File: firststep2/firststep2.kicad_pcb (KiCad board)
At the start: 2 copper layers, 43.2 x 17.8 mm, 43 parts, among them J1 Analog, J10 Arduino_A7, J11 Arduino_D6, J12 RELAY_SW, J13 RELAY_PWR, J14 Arduino_D9, J15 Conn_FET, J2 Conn_01x03_Male, J2 Digital, J3 POWER12, J4 Conn_5V, J5 Conn_GND, J6 Arduino_A6, U1 LM317_TO-220, U2 TL072, U2 TL431LP, U4 MIC4428

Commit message: update pcb
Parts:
- removed the R6 at (231.8, 66.8)
- removed the R7 at (248.6, 122.9)
- R5: value 220 -> 1K
- RV1: value R_Potentiometer -> 20K; footprint Potentiometer_THT:Potentiometer_Bourns_3386F_Vertical -> Potentiometer_THT:Potentiometer_Vishay_T73YP_Vertical
- moved R2 145.7 mm to (263.4, 53.8)
- moved C2 131.3 mm to (270.2, 57.8)
- moved R2 126.9 mm to (259.4, 57.8), turned to 0 degrees
- moved R6 117.6 mm to (226.0, 50.2), turned to -90 degrees
- moved U2 116.7 mm to (271.3, 65.7), turned to 180 degrees
- moved D1 107.3 mm to (267.0, 60.8), turned to 180 degrees
- moved C4 106.0 mm to (261.2, 43.0), turned to -90 degrees
- moved R3 96.7 mm to (263.2, 34.6)
- moved U1 96.3 mm to (263.7, 38.0), turned to 180 degrees
- moved J13 88.2 mm to (173.0, 55.0)
- moved U4 87.9 mm to (241.8, 56.8), turned to 180 degrees
- moved R7 85.8 mm to (232.8, 34.0), turned to 180 degrees
- moved R5 83.7 mm to (271.0, 47.8), turned to 90 degrees
- moved U2 81.9 mm to (274.0, 48.0)
- moved R4 81.7 mm to (268.0, 47.8), turned to 90 degrees
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- renumbered R12 to R10, R13 to R11, R14 to R12, R8 to R6, R9 to R7, R11 to R9
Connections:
- C5 pad 1: GND -> /accel/A6
- C5 pad 2: /accel/A6 -> GND
- R5 pad 1: Net-(R5-Pad1) -> /accel/amp
- RV1 pad 1: Net-(RV1-Pad1) -> GND
- RV1 pad 3: GND -> Net-(RV1-Pad3)
- U2 pad 1: Net-(RV1-Pad1) -> Net-(RV1-Pad3)
- U2 pad 2: Net-(RV1-Pad1) -> Net-(RV1-Pad3)
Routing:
- net GND: track 0.00 -> 67.2 mm
- net /accel/amp: track 0.00 -> 56.4 mm
- net Net-(C4-Pad1): track 0.00 -> 51.2 mm
- net Net-(C3-Pad1): track 0.00 -> 17.0 mm
- net Net-(RV1-Pad3): track 0.00 -> 8.57 mm
- net Net-(C2-Pad1): track 0.00 -> 8.31 mm
- net +5V: track 0.00 -> 8.03 mm
- net /accel/A6: track 0.00 -> 6.65 mm
- net Net-(J12-Pad2): track 0.00 -> 6.38 mm
- net Net-(R2-Pad2): track 0.00 -> 3.31 mm
- net /driver/*D6: track 0.00 -> 3.19 mm
- added copper zone on B.Cu, net GND
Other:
- board size 43.2 x 17.8 mm -> 75 x 74 mm

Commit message: update pcb
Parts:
- J13: footprint Connector_PinHeader_2.54mm:PinHeader_1x01_P2.54mm_Vertical -> Connector_PinHeader_2.54mm:PinHeader_1x02_P2.54mm_Vertical
- moved J6 187.9 mm to (108.7, 127.2), turned to 90 degrees
- moved C5 179.8 mm to (113.2, 112.2), turned to 90 degrees
- moved J4 179.7 mm to (108.8, 130.1), turned to 90 degrees
- moved RV1 174.1 mm to (119.2, 111.2), turned to 180 degrees
- moved R3 173.7 mm to (113.7, 123.0), turned to 90 degrees
- moved U1 172.9 mm to (115.2, 126.5), turned to -90 degrees
- moved R7 167.7 mm to (95.4, 130.2), turned to 0 degrees
- moved C4 165.2 mm to (120.2, 129.0), turned to 0 degrees
- moved U2 163.7 mm to (125.2, 116.2), turned to 90 degrees
- moved R5 162.5 mm to (125.0, 119.2), turned to 180 degrees
- moved C3 162.1 mm to (123.2, 126.0), turned to 0 degrees
- moved R4 161.2 mm to (125.0, 122.2), turned to 180 degrees
- moved C1 160.1 mm to (123.2, 132.0), turned to 0 degrees
- moved R12 159.3 mm to (100.9, 111.2), turned to 0 degrees
- moved C6 157.4 mm to (98.7, 133.2), turned to 180 degrees
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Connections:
- D1 pad 1: GND -> /accel/amp
- D1 pad 2: /accel/amp -> GND
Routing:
- net GND: track 67.2 -> 199.7 mm
- net VCC: track 0.00 -> 56.1 mm
- net /accel/A6: track 6.65 -> 20.9 mm
- net /accel/A7: track 0.00 -> 12.4 mm
- net /accel/amp: track 56.4 -> 44.1 mm
- net Net-(C4-Pad1): track 51.2 -> 41.1 mm
- net /driver/*D9: track 0.00 -> 7.90 mm
- net +5V: track 8.03 -> 14.6 mm
- net /driver/*D6: track 3.19 -> 9.05 mm
- net Net-(R12-Pad2): track 0.00 -> 4.18 mm
- net Net-(J15-Pad1): track 0.00 -> 3.29 mm
- net Net-(J12-Pad2): track 6.38 -> 8.60 mm
- net Net-(C3-Pad1): track 17.0 -> 15.7 mm
- net (no net): vias 0 -> 11
- removed copper zone on B.Cu, net GND
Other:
- board size 75 x 74 mm -> 53 x 63 mm

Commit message: minor pcb
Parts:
- moved J15 1.72 mm to (96.0, 120.2)
- moved J3 1.72 mm to (96.0, 123.2)
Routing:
- net Net-(J15-Pad1): track 3.29 -> 5.01 mm
- net VCC: track 56.1 -> 55.4 mm
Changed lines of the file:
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@@
   )
   (footprint "Connector_PinHeader_2.54mm:PinHeader_1x01_P2.54mm_Vertical" (layer "F.Cu")
-    (at 97.725 120.185 90)
+    (at 96 120.185 90)
     (descr "Through hole straight pin header, 1x01, 2.54mm pitch, single row")
     (tags "Through hole pin header THT 1x01 2.54mm single row")
@@
   )
   (footprint "Connector_PinHeader_2.54mm:PinHeader_1x01_P2.54mm_Vertical" (layer "F.Cu")
-    (at 97.725 123.185 90)
+    (at 96 123.185 90)
     (descr "Through hole straight pin header, 1x01, 2.54mm pitch, single row")
     (tags "Through hole pin header THT 1x01 2.54mm single row")
@@
   (segment (start 125.685 134.225) (end 114.725 134.185) (width 0.6) (layer "B.Cu") (net 1))
   (segment (start 101.805 111.185) (end 100.915 111.185) (width 0.6) (layer "B.Cu") (net 1))
-  (segment (start 98.120002 117.905) (end 100.905 117.905) (width 0.6) (layer "B.Cu") (net 3))
+  (segment (start 95.415 123.77) (end 96 123.185) (width 0.6) (layer "B.Cu") (net 3))
+  (segment (start 95.415 127.185) (end 95.415 123.77) (width 0.6) (layer "B.Cu") (net 3))
   (segment (start 94.115 128.485) (end 94.115 136.575) (width 0.6) (layer "B.Cu") (net 3))
   (segment (start 98.725 141.185) (end 108.725 141.185) (width 0.6) (layer "B.Cu") (net 3))
   (segment (start 95.415 127.185) (end 98.815 127.185) (width 0.6) (layer "B.Cu") (net 3))
   (segment (start 108.725 141.185) (end 108.725 139.185) (width 0.6) (layer "B.Cu") (net 3))
-  (segment (start 97.725 124.875) (end 95.415 127.185) (width 0.6) (layer "B.Cu") (net 3))
   (segment (start 94.115 136.575) (end 98.725 141.185) (width 0.6) (layer "B.Cu") (net 3))
-  (segment (start 98.120002 114.580002) (end 98.120002 117.905) (width 0.6) (layer "B.Cu") (net 3))
   (segment (start 98.815 127.185) (end 102.205 123.795) (width 0.6) (layer "B.Cu") (net 3))
   (segment (start 95.415 127.185) (end 94.115 128.485) (width 0.6) (layer "B.Cu") (net 3))
-  (segment (start 97.725 123.185) (end 97.725 124.875) (width 0.6) (layer "B.Cu") (net 3))
+  (segment (start 98.120002 114.580002) (end 98.120002 117.905) (width 0.6) (layer "B.Cu") (net 3))
+  (segment (start 100.905 117.905) (end 98.120002 117.905) (width 0.6) (layer "B.Cu") (net 3))
   (segment (start 102.205 119.205) (end 100.905 117.905) (width 0.6) (layer "B.Cu") (net 3))
   (segment (start 96.725 113.185) (end 98.120002 114.580002) (width 0.6) (layer "B.Cu") (net 3))
@@
   (segment (start 108.525 120.445) (end 105.725 123.245) (width 0.6) (layer "B.Cu") (net 37))
   (segment (start 105.725 123.245) (end 105.725 127.185) (width 0.6) (layer "B.Cu") (net 37))
-  (segment (start 100.905 120.445) (end 97.985 120.445) (width 0.6) (layer "B.Cu") (net 38))
-  (segment (start 97.985 120.445) (end 97.725 120.185) (width 0.6) (layer "B.Cu") (net 38))
+  (segment (start 100.905 120.445) (end 96.26 120.445) (width 0.6) (layer "B.Cu") (net 38))
+  (segment (start 96.26 120.445) (end 96 120.185) (width 0.6) (layer "B.Cu") (net 38))
   (segment (start 131 119.19) (end 131 116.92) (width 0.6) (layer "B.Cu") (net 39))
   (segment (start 131 116.92) (end 130.265 116.185) (width 0.6) (layer "B.Cu") (net 39))

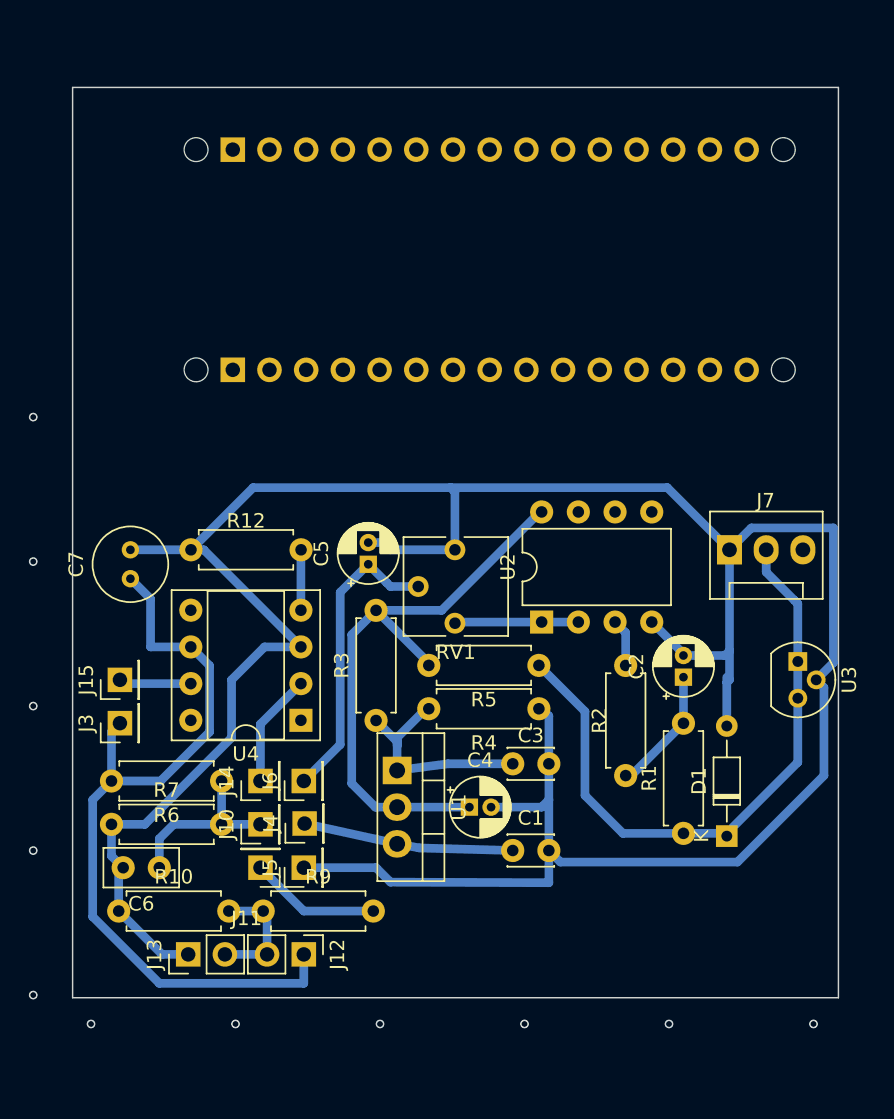
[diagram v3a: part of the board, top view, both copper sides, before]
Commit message: added NE555 50kHz gen
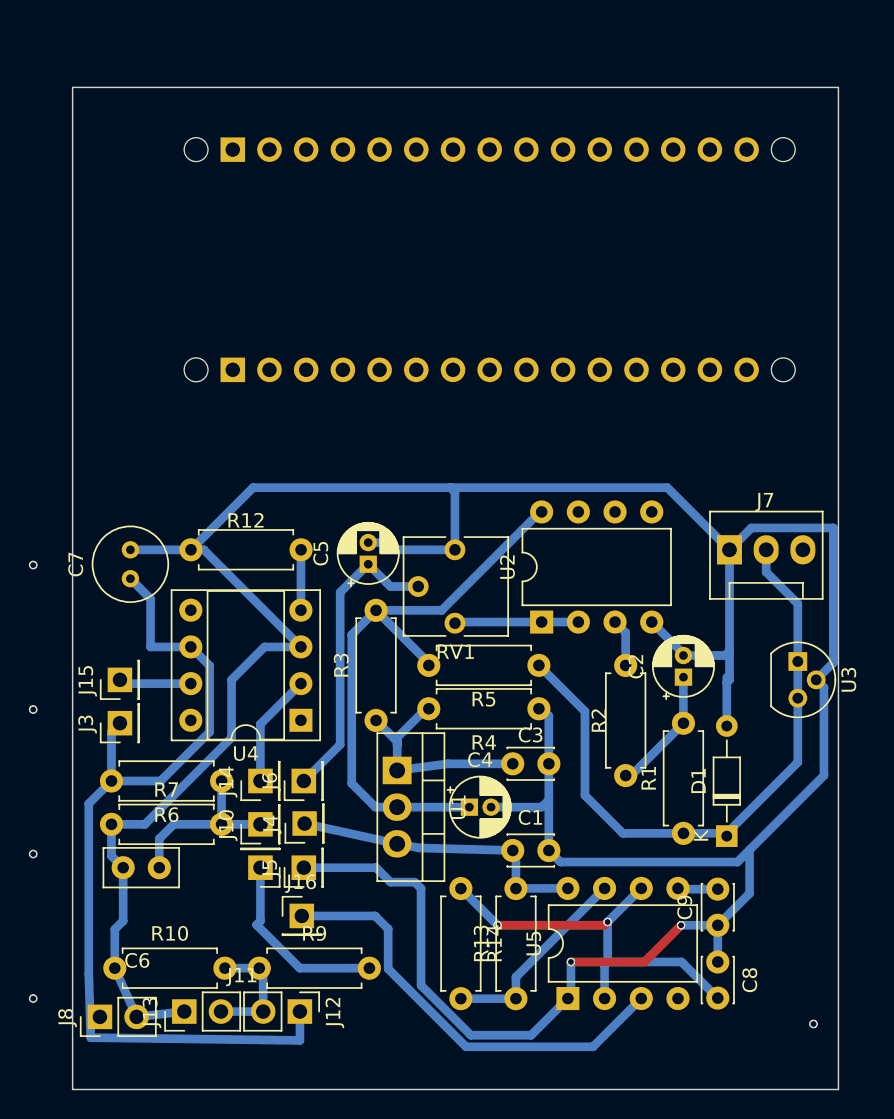
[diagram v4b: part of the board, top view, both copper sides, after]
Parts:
- added C8: 6.8n, Capacitor_THT:C_Disc_D3.0mm_W2.0mm_P2.50mm, F.Cu at (137.4, 139.7)
- added C9: 10n, Capacitor_THT:C_Disc_D3.0mm_W2.0mm_P2.50mm, F.Cu at (137.4, 137.2)
- added J16: Arduino_RX0, Connector_PinHeader_2.54mm:PinHeader_1x01_P2.54mm_Vertical, F.Cu at (108.6, 136.5)
- added J8: BACKLAMP, Connector_PinHeader_2.54mm:PinHeader_1x02_P2.54mm_Vertical, F.Cu at (94.6, 143.5)
- added R13: 1K, Resistor_THT:R_Axial_DIN0207_L6.3mm_D2.5mm_P7.62mm_Horizontal, F.Cu at (123.4, 142.2)
- added R14: 1K, Resistor_THT:R_Axial_DIN0207_L6.3mm_D2.5mm_P7.62mm_Horizontal, F.Cu at (119.6, 134.6)
- added U5: NE555P, Package_DIP:DIP-8_W7.62mm, F.Cu at (127.0, 142.2)
- moved R10 3.96 mm to (95.6, 140.1)
- moved R9 3.96 mm to (105.6, 140.1)
- moved J12 3.96 mm to (108.5, 143.1)
- moved J13 3.96 mm to (100.5, 143.1)
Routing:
- net GND: track 199.7 -> 236.1 mm, vias 0 -> 2
- net /D1/TX: track 0.00 -> 30.2 mm
- net Net-(U5-Pad2): track 0.00 -> 28.9 mm, vias 0 -> 2
- net Net-(U5-Pad7): track 0.00 -> 14.5 mm
- net VCC: track 55.4 -> 63.5 mm
- net +5V: track 14.6 -> 21.1 mm
- net /driver/*D6: track 9.05 -> 13.1 mm
- net Net-(U5-Pad5): track 0.00 -> 2.78 mm
- net (no net): vias 11 -> 5
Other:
- board size 53 x 63 mm -> 53 x 69.3 mm
